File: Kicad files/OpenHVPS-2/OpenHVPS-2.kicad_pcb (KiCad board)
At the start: 2 copper layers, 47.1 x 20.5 mm, 69 parts, among them J1 Conn_01x03_Male, J2 Conn_01x03_Male, Q1 FQT7N10, Q2 BC846, Q3 MMDT3906, U1 MAX6008AEUR+T, U2 74HC14, U3 MAX4162, U4 CD14538BM

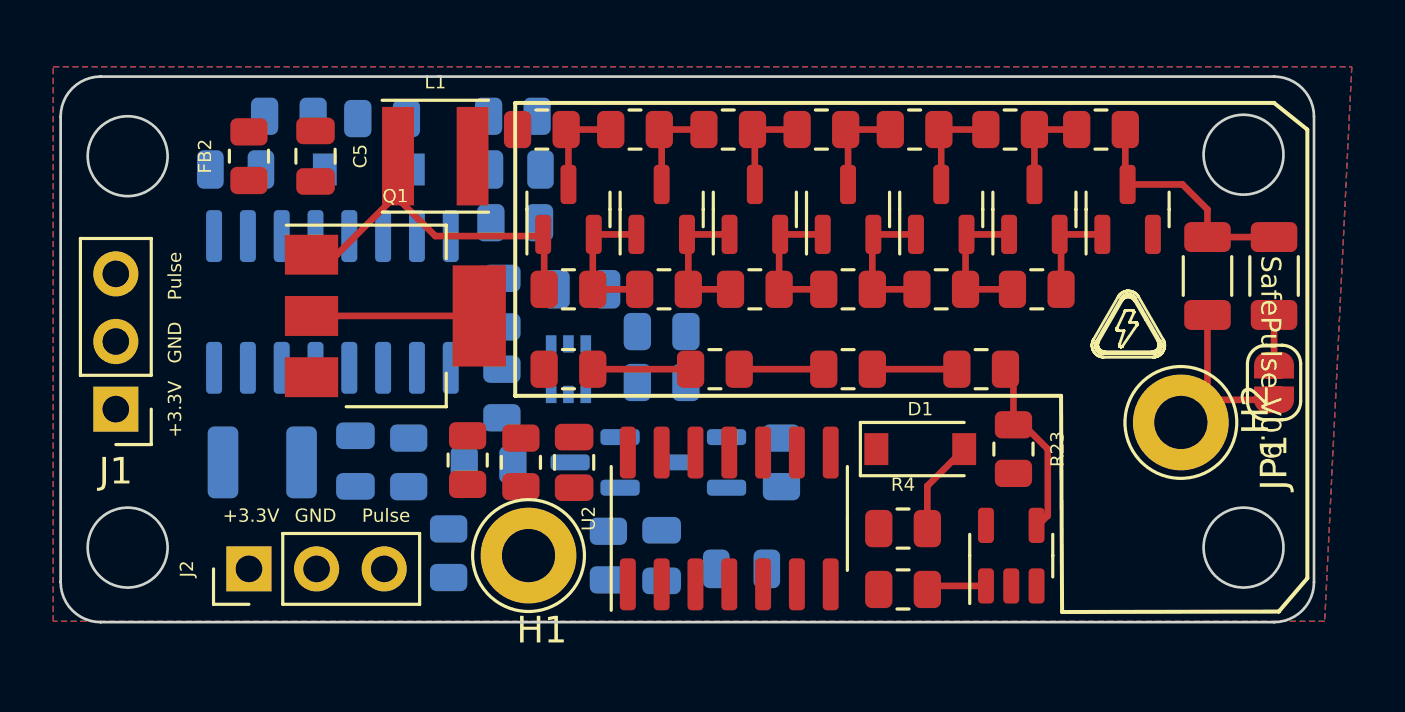
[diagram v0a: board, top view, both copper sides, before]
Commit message: Change the diodes
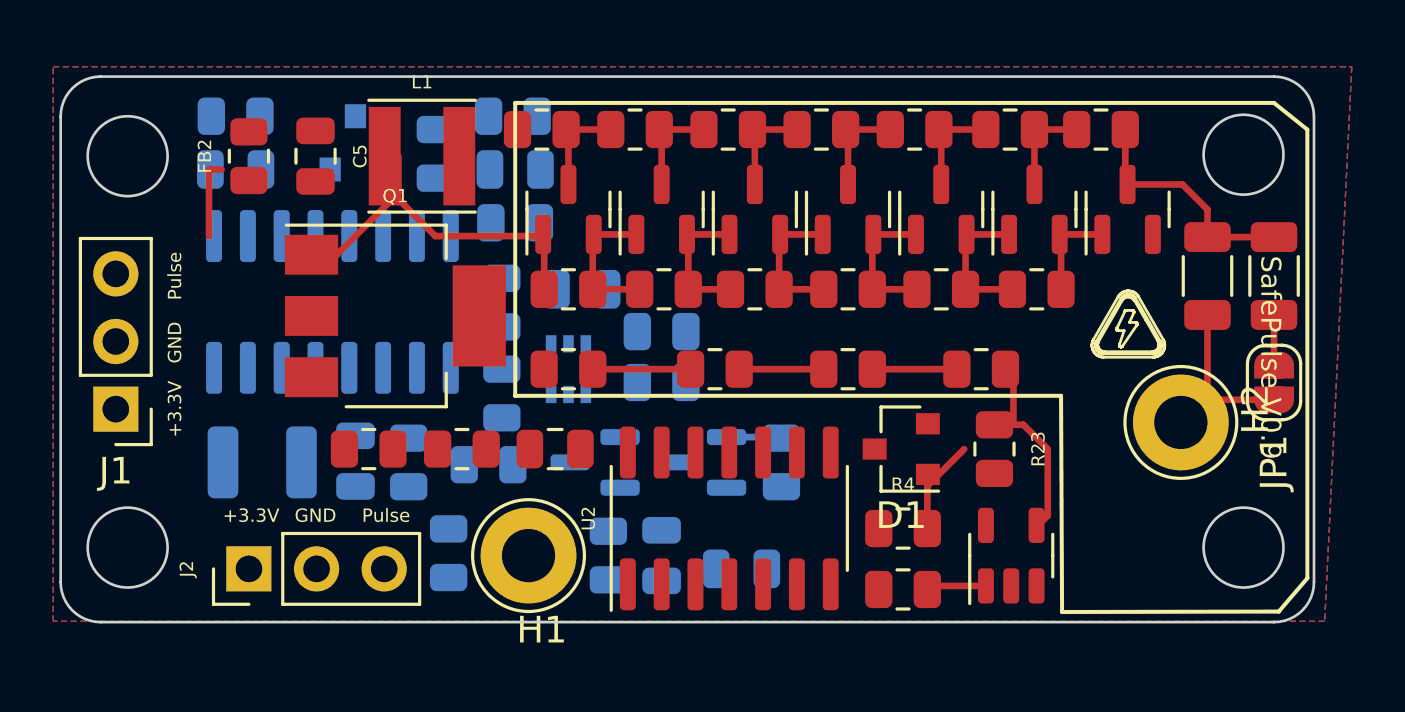
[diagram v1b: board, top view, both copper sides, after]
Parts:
- D1, D2: value 1N4148W -> BAS16; footprint Diode_SMD:D_SOD-123 -> Diode_SMD:D_SOT-23_ANK
- moved FB1 3.74 mm to (132.5, 71.0), turned to 0 degrees
- moved R11 2.40 mm to (135.0, 59.9), turned to 90 degrees
- moved R5 2.27 mm to (136.0, 71.0), turned to 180 degrees
- moved R6 2.00 mm to (127.5, 58.5)
- moved D2 1.12 mm to (132.0, 59.5), turned to 90 degrees
- moved C2 0.87 mm to (139.5, 71.0), turned to 0 degrees
- moved D1 0.71 mm to (152.5, 71.0), turned to 180 degrees
- moved R23 0.71 mm to (156.0, 71.0)
- moved L1 0.50 mm to (134.5, 60.0)
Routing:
- net Net-(Q1-Pad2): track 6.30 -> 0.00 mm
- net (no net): track 0.00 -> 2.97 mm
- net +2V5: track 0.00 -> 2.08 mm

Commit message: Routed draft version
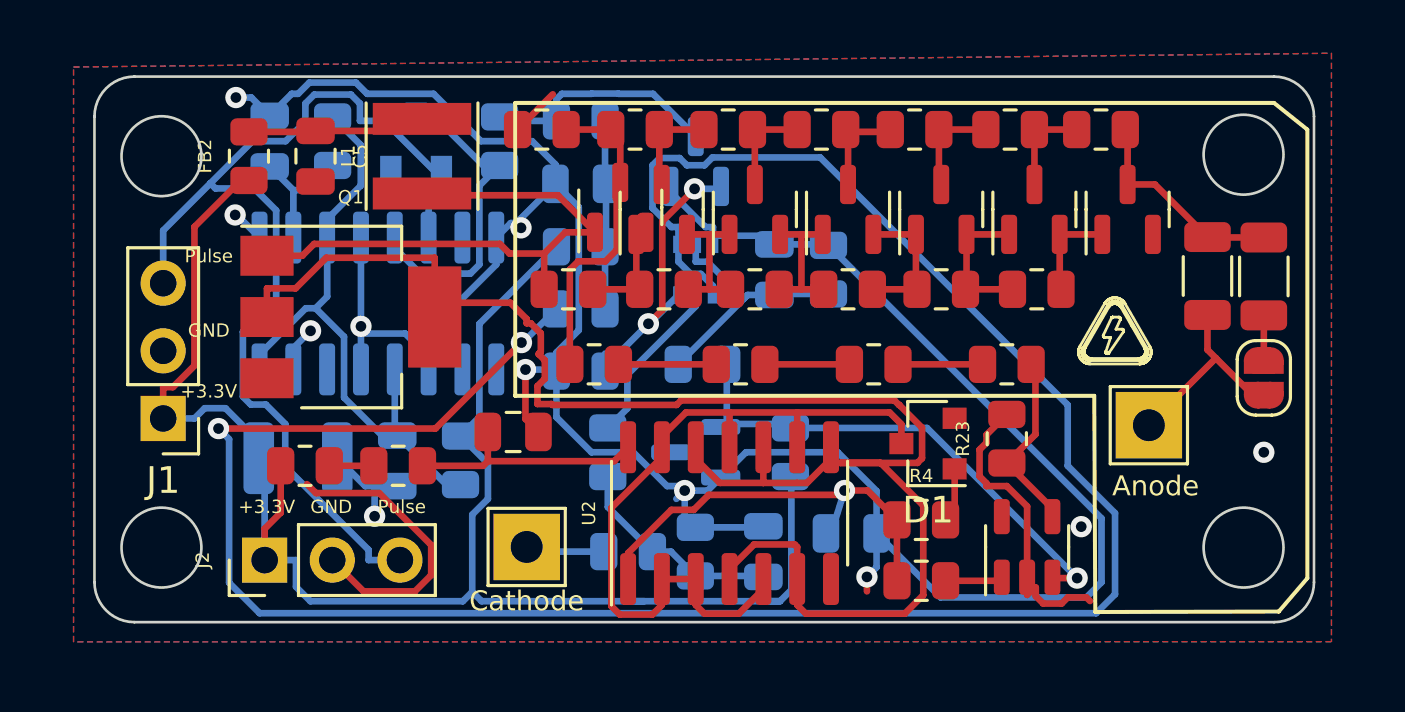
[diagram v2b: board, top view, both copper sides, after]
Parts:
- H1, H2: footprint TestPoint:TestPoint_Loop_D3.80mm_Drill2.0mm -> TestPoint:TestPoint_THTPad_2.5x2.5mm_Drill1.2mm
- moved Q2 11.9 mm to (144.8, 60.2), turned to 90 degrees
- moved C15 7.27 mm to (147.7, 64.3), turned to 90 degrees
- moved R21 6.74 mm to (142.2, 74.9), turned to 0 degrees
- moved R15 6.68 mm to (149.8, 64.3), turned to 90 degrees
- moved Q3 6.07 mm to (144.8, 64.3)
- moved R19 4.50 mm to (141.5, 71.1), turned to -90 degrees
- moved C1 4.33 mm to (150.6, 74.2)
- moved C22 3.82 mm to (147.3, 74.9), turned to 90 degrees
- moved R6 3.76 mm to (131.1, 59.4), turned to -90 degrees
- moved R22 3.27 mm to (144.8, 74.9), turned to 90 degrees
- moved R16 3.08 mm to (140.5, 68.1), turned to 180 degrees
- moved R17 2.97 mm to (140.5, 65.7), turned to 180 degrees
- moved R18 2.62 mm to (140.5, 63.4)
- moved R13 2.56 mm to (140.5, 58.7)
- moved C19 2.52 mm to (140.5, 61.0)
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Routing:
- net GND: track 0.00 -> 133.9 mm, vias 0 -> 11
- net Net-(Q3-Pad1): track 0.00 -> 88.4 mm, vias 0 -> 2
- net +3V3: track 0.00 -> 65.2 mm
- net Net-(Q1-Pad2): track 0.00 -> 63.0 mm
- net Net-(D2-Pad2): track 0.00 -> 39.4 mm
- net Net-(D1-Pad1): track 0.00 -> 28.9 mm
- net Net-(C10-Pad1): track 0.00 -> 23.8 mm
- net +2V5: track 2.08 -> 19.0 mm, vias 0 -> 1
- net Net-(C1-Pad1): track 0.00 -> 16.9 mm, vias 0 -> 1
- net Net-(D2-Pad1): track 0.00 -> 12.1 mm
- net Net-(Q2-Pad1): track 0.00 -> 11.9 mm, vias 0 -> 2
- net Net-(C15-Pad1): track 0.00 -> 9.78 mm
- net Net-(C2-Pad1): track 0.00 -> 9.11 mm
- net Net-(Q2-Pad3): track 0.00 -> 9.00 mm
- net Net-(C6-Pad2): track 3.77 -> 12.0 mm
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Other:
- board size 47.1 x 20.5 mm -> 45.8 x 20.5 mm

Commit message: One more rerout to cleanup.
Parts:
- moved D3 1.99 mm to (140.0, 62.0)
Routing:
- net Net-(Q3-Pad1): track 88.4 -> 9.80 mm, vias 2 -> 0
- net GND: track 133.9 -> 107.1 mm, vias 11 -> 10
- net Net-(Q2-Pad1): track 11.9 -> 18.4 mm
- net Net-(C7-Pad1): track 21.4 -> 15.5 mm
- net Net-(C7-Pad2): track 4.20 -> 5.64 mm
- net Net-(C1-Pad1): track 16.9 -> 18.2 mm
- net Net-(Q3-Pad5): track 6.36 -> 7.35 mm
- net Net-(C15-Pad1): track 9.78 -> 10.6 mm
- net Net-(C6-Pad2): track 12.0 -> 12.6 mm

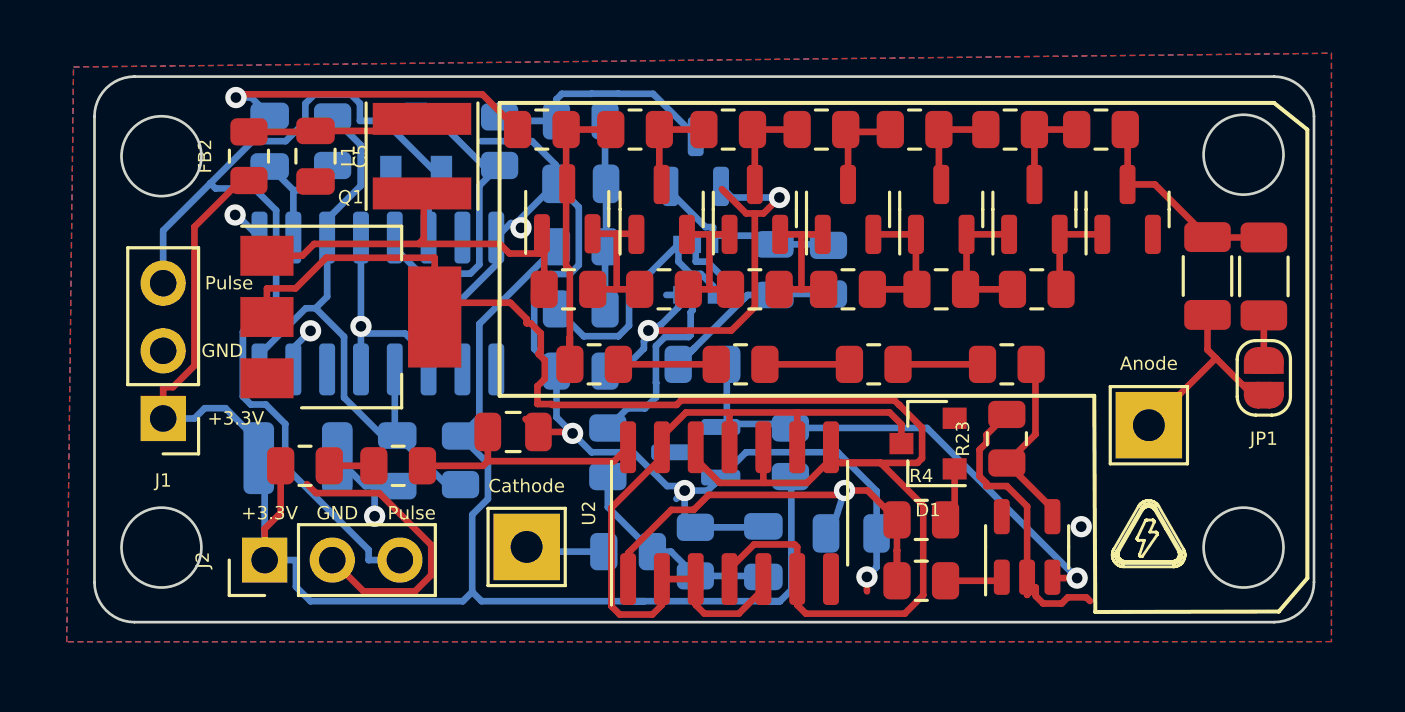
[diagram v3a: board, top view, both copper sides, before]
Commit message: Sanity checks, parts shuffling, optimize copper pours
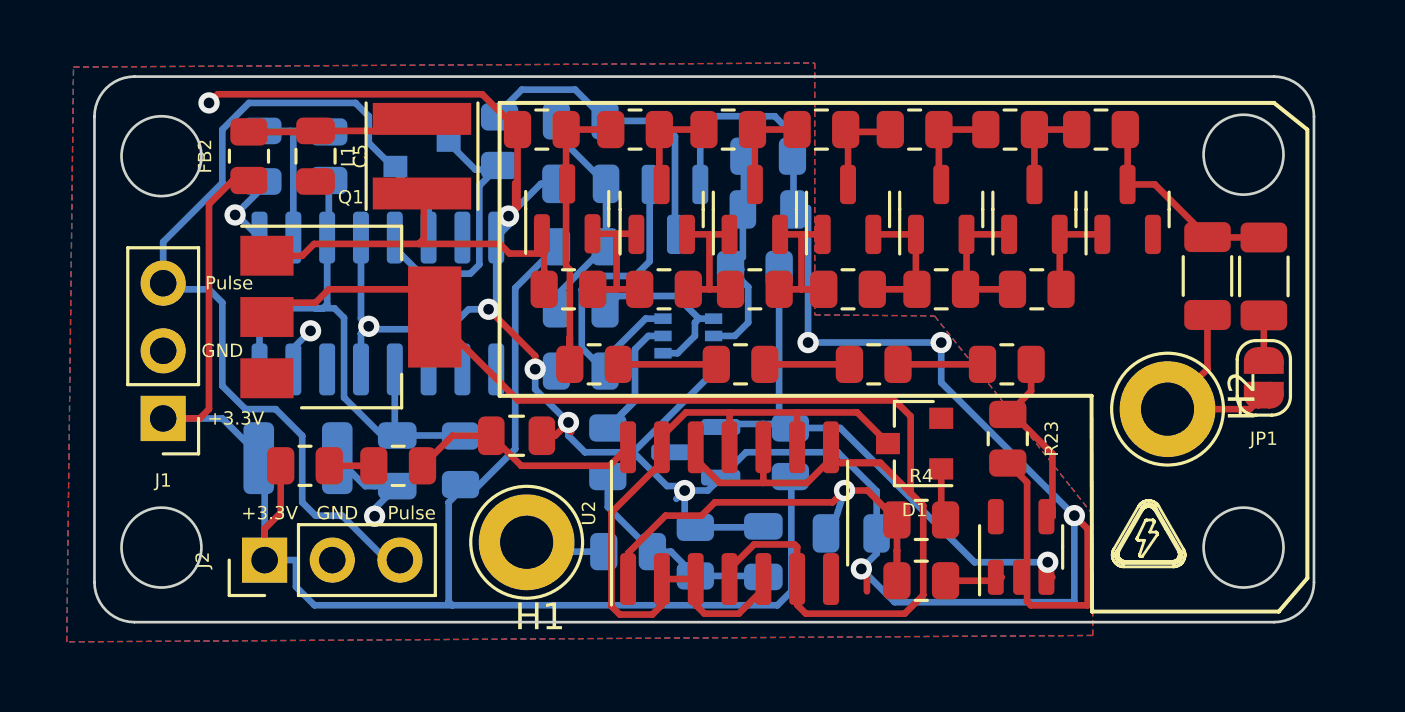
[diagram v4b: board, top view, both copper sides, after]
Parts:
- H1, H2: footprint TestPoint:TestPoint_THTPad_2.5x2.5mm_Drill1.2mm -> TestPoint:TestPoint_Loop_D3.80mm_Drill2.0mm
- JP1: value SolderJumper_2_Open -> 7317
- R5: value R -> 100
- moved R15 4.83 mm to (147.5, 60.0), turned to 0 degrees
- moved R14 4.07 mm to (147.0, 64.2)
- moved Q3 2.50 mm to (144.5, 66.8), turned to 180 degrees
- moved C15 2.27 mm to (147.5, 62.0), turned to 0 degrees
- moved Q2 1.96 mm to (144.0, 62.0), turned to -90 degrees
- moved H2 0.93 mm to (162.5, 69.5)
- moved C3 0.63 mm to (128.5, 60.0), turned to -90 degrees
- moved R6 0.58 mm to (131.0, 60.0), turned to 90 degrees
- moved D1 0.50 mm to (153.0, 70.8)
- moved U3 0.23 mm to (157.0, 74.7)
- moved D2 0.22 mm to (134.5, 59.4), turned to 0 degrees
- moved C2 0.19 mm to (138.1, 70.5)
- moved H1 0.18 mm to (138.4, 74.5)
- turned R23 to -90 degrees
- turned R12 to 90 degrees
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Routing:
- net GND: track 107.1 -> 131.4 mm, vias 10 -> 14
- net Net-(Q2-Pad1): track 18.4 -> 13.4 mm, vias 2 -> 0
- net Net-(Q1-Pad2): track 63.0 -> 58.2 mm
- net Net-(D2-Pad2): track 39.4 -> 34.6 mm
- net Net-(Q2-Pad3): track 9.00 -> 11.8 mm
- net Net-(C19-Pad1): track 7.10 -> 9.79 mm
- net Net-(Q3-Pad1): track 9.80 -> 7.17 mm
- net Net-(C10-Pad1): track 23.8 -> 21.3 mm
- net Net-(C15-Pad1): track 10.6 -> 8.33 mm
- net +2V5: track 19.0 -> 21.3 mm
- net Net-(Q3-Pad5): track 7.35 -> 5.39 mm
- net Net-(C3-Pad1): track 4.90 -> 6.57 mm
- net Net-(D2-Pad1): track 12.1 -> 10.6 mm
- net Net-(D1-Pad1): track 28.9 -> 28.0 mm

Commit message: BOM mostly done. cleaned up component labels
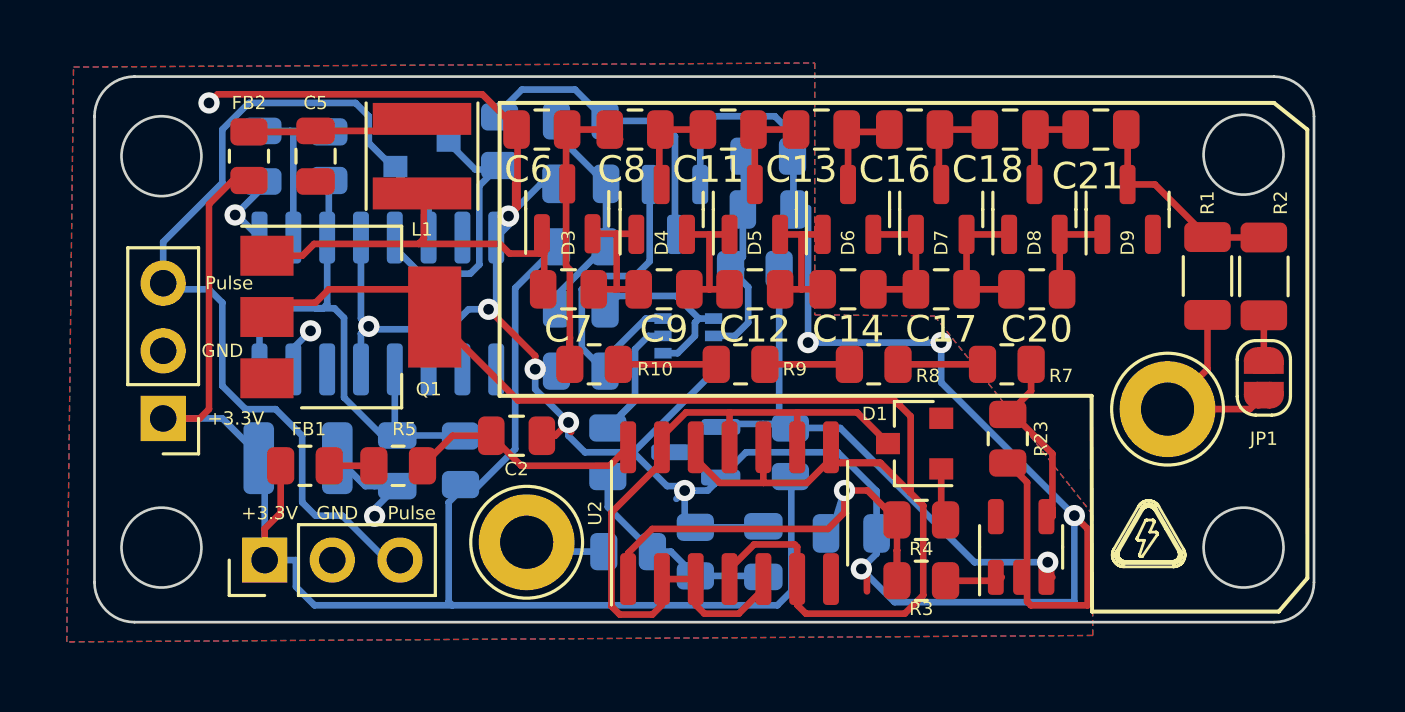
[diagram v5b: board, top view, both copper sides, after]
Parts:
- C1: value 0.1 -> 0.1uF
- C11, C12, C13, C14, C16, C17, C18, C20, C21, C6, C7, C8, C9: value 0.1 -> 0.1uF; footprint Resistor_SMD:R_0805_2012Metric -> Capacitor_SMD:C_0805_2012Metric
- C15, C22: value C -> 1nF
- C19: value C -> 0.1uF
- FB1, FB2: value Ferrite_Bead -> BKP2125HS221-T
- L1: value 2.2uH -> NRS6020T2R2NMGJ
- Q2: value BC846 -> BC846A

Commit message: Created BOM. updated component markings
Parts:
- R14: value 1M49 -> 1M5
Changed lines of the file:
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@@
       (effects (font (size 0.5 0.5) (thickness 0.075)) (justify mirror))
     )
-    (fp_text value "1M49" (at 0 -1.65) (layer "B.Fab") hide
+    (fp_text value "1M5" (at 0 -1.65) (layer "B.Fab") hide
       (effects (font (size 0.5 0.5) (thickness 0.075)) (justify mirror))
     )
